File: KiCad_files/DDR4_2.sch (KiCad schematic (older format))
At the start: 16 parts

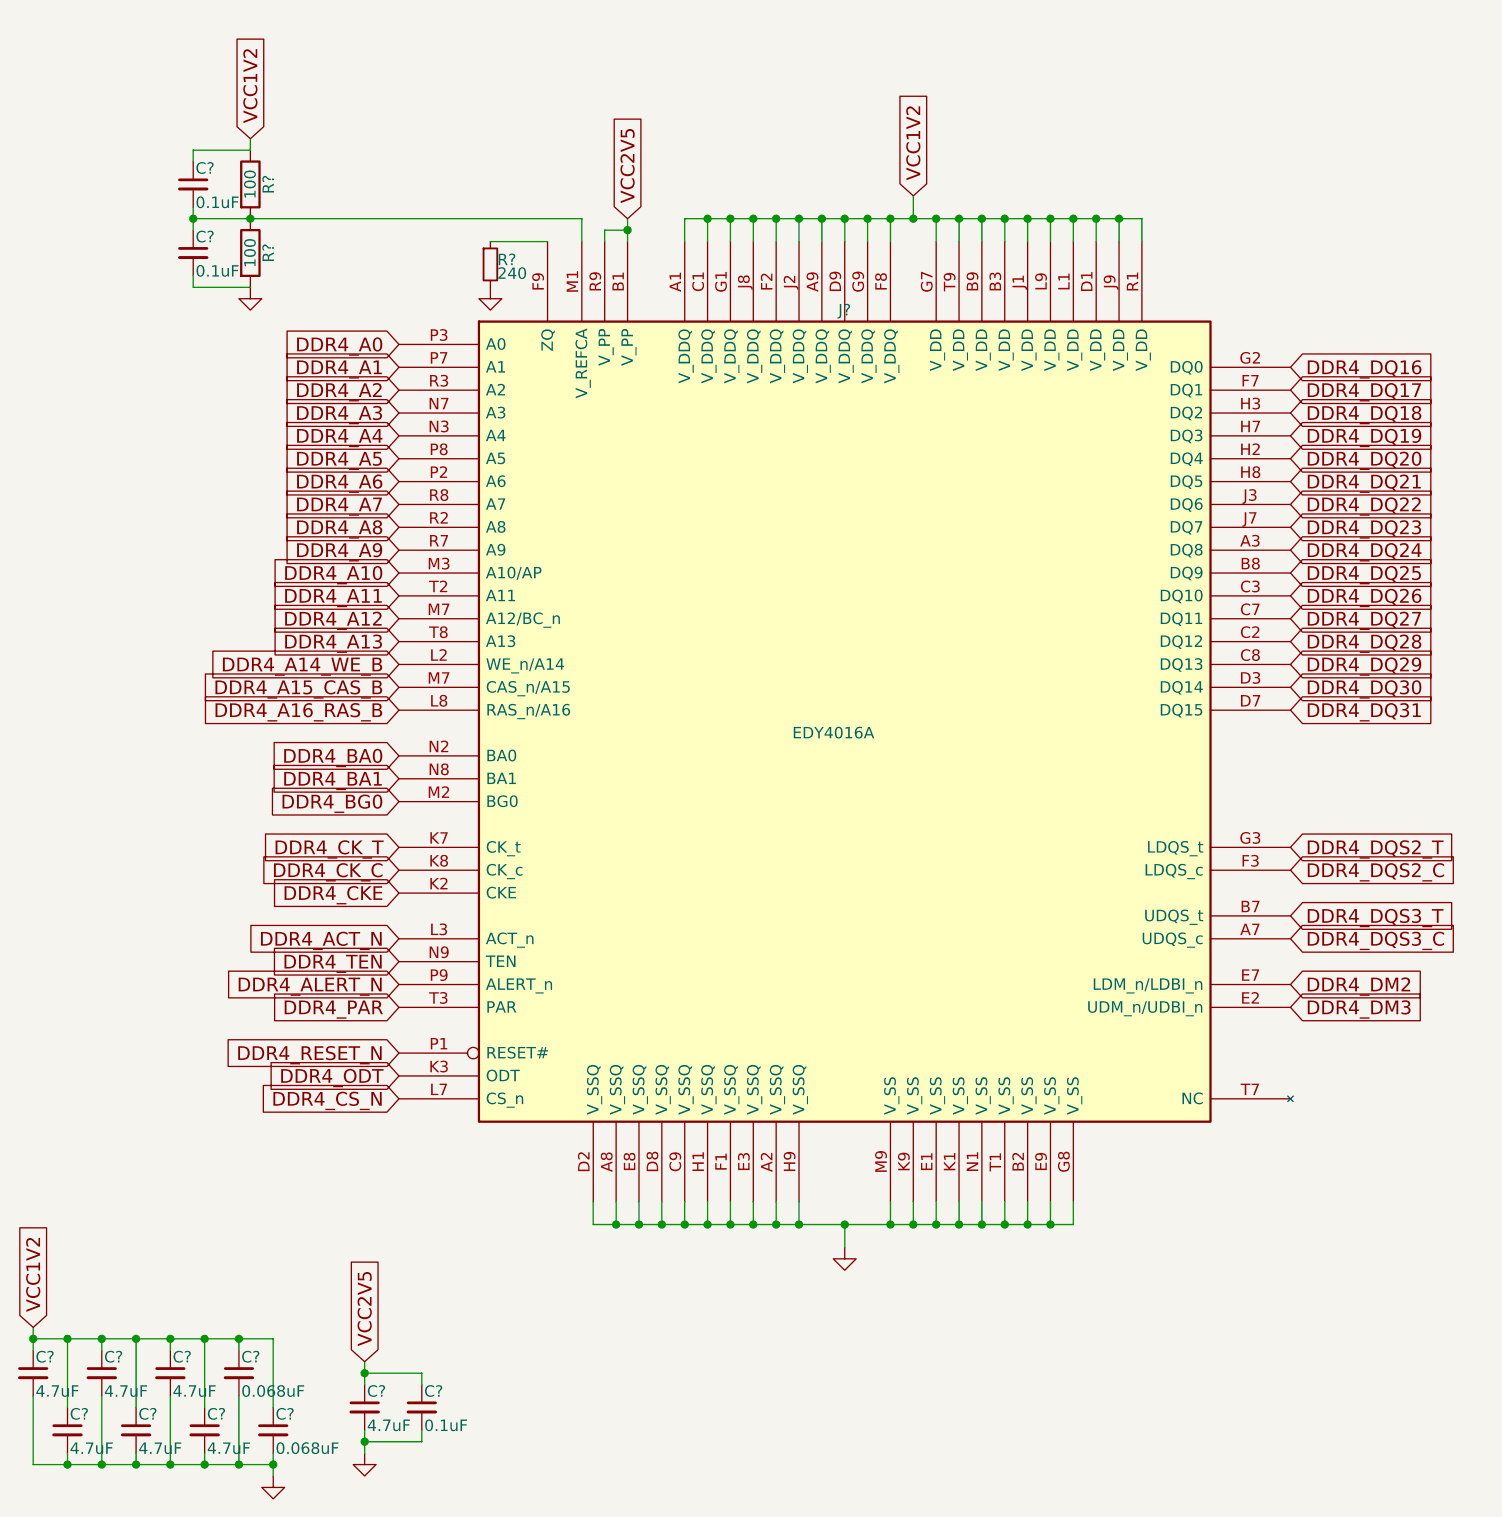
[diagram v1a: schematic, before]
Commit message: Cleanup for demo/presentation
Merged Config and Debug sheets.
Added GPIO for remaining pins.
Annotations.
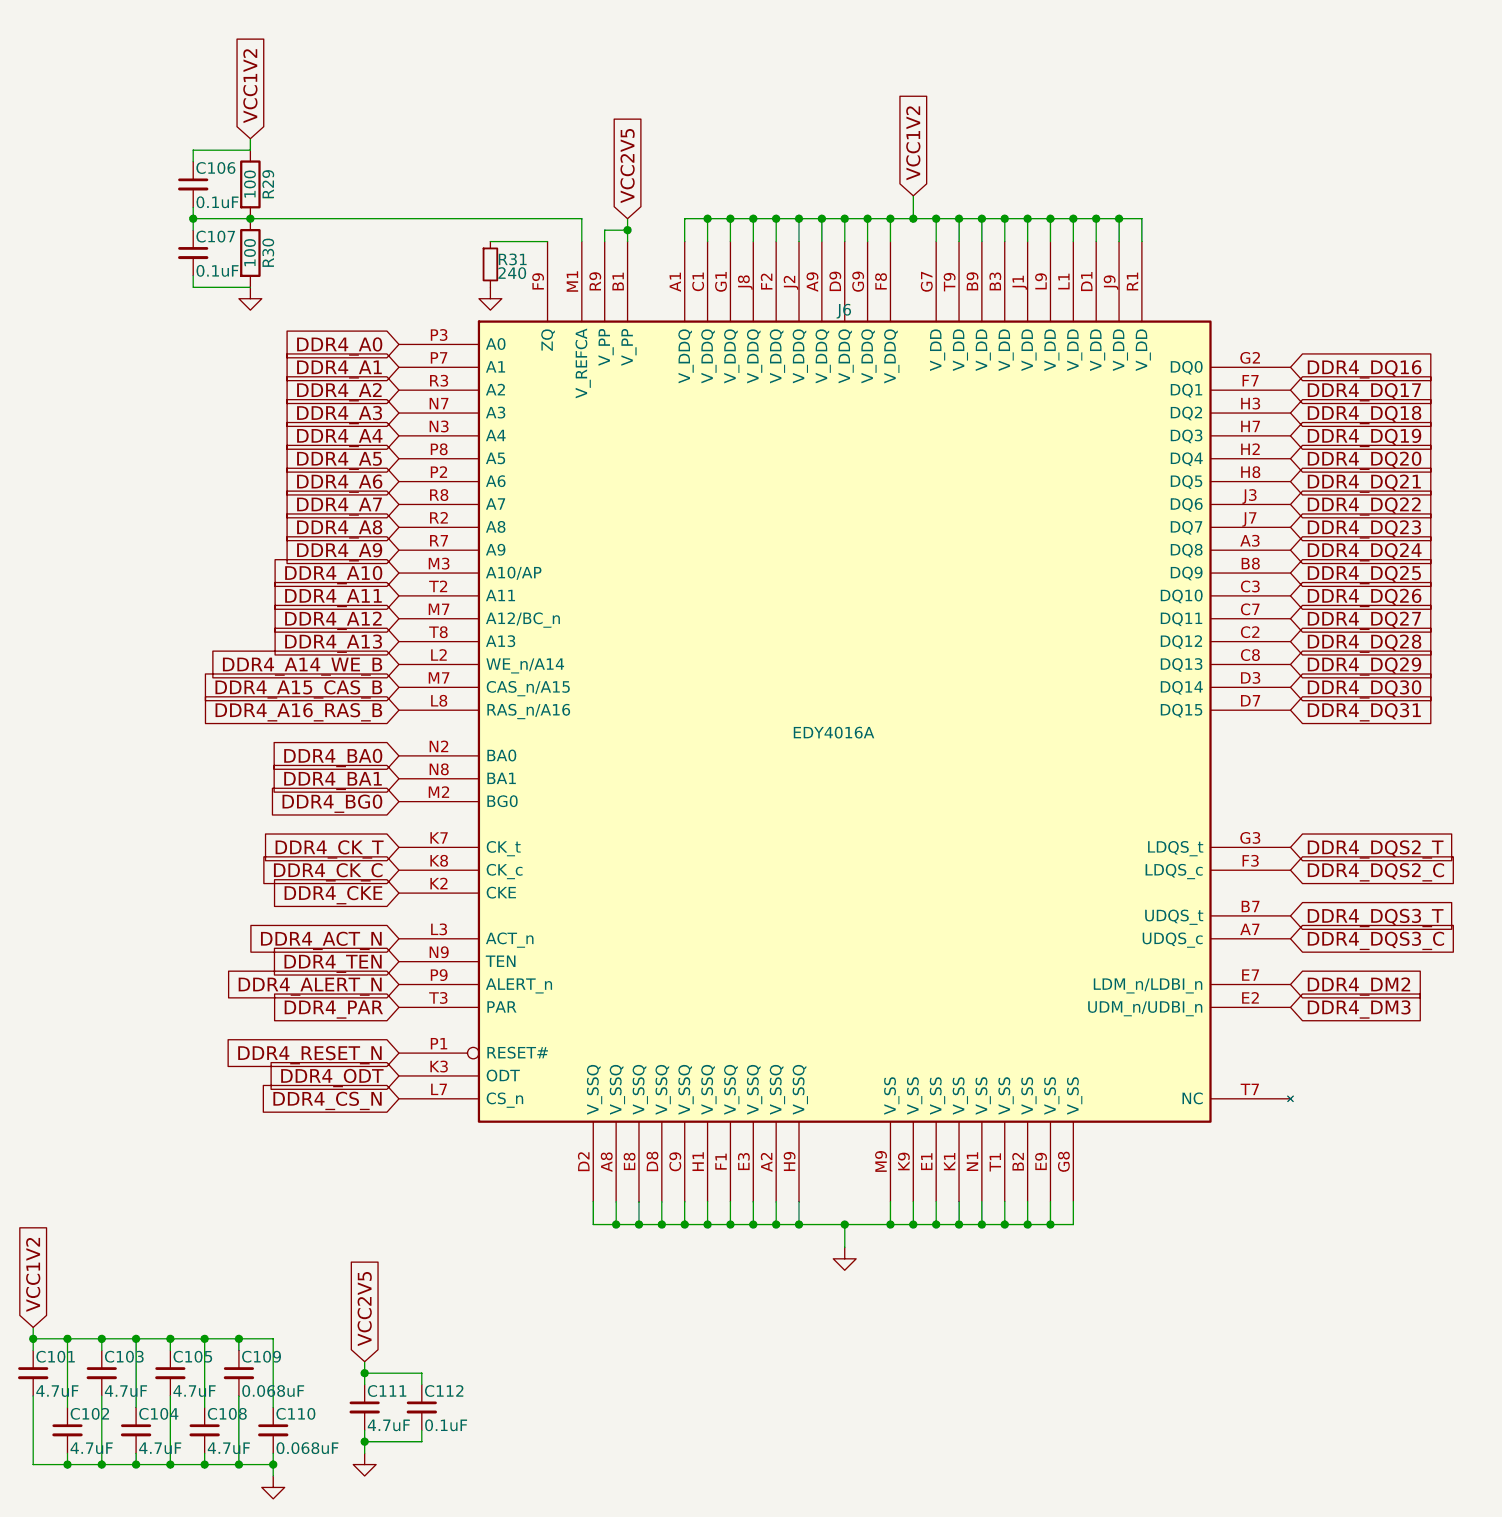
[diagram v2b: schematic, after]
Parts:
- gave numbers to parts that had none: 16
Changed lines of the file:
@@
 $Descr A4 11693 8268
 encoding utf-8
-Sheet 9 10
-Title ""
-Date ""
-Rev ""
-Comp ""
+Sheet 8 10
+Title "Reconfigurable Application-Specific Accelerator Card"
+Date "2018-11-27"
+Rev "1.0"
+Comp "Brian Hong & Jasmine Tang"
 Comment1 ""
-Comment2 ""
-Comment3 ""
-Comment4 ""
+Comment2 "Advisor: Professor Sable"
+Comment3 "Senior Projects"
+Comment4 "The Cooper Union for the Advancement of Science and Art"
 $EndDescr
 $Comp
-L EDY4016A J?
+L EDY4016A J6
 U 1 1 5C14AF0F
 P 6100 4000
-F 0 "J?" H 6100 5850 50  0000 C CNN
+F 0 "J6" H 6100 5850 50  0000 C CNN
 F 1 "EDY4016A" H 6050 4000 50  0000 C CNN
 F 2 "" H 6100 2650 50  0001 C CNN
@@
 VCC2V5
 $Comp
-L R_Small R?
+L R_Small R31
 U 1 1 5C14AF28
 P 4550 1950
-F 0 "R?" H 4580 1970 50  0000 L CNN
+F 0 "R31" H 4580 1970 50  0000 L CNN
 F 1 "240" H 4580 1910 50  0000 L CNN
 F 2 "" H 4550 1950 50  0001 C CNN
@@
 $EndComp
 $Comp
-L GND #PWR?
+L GND #PWR102
 U 1 1 5C14AF2F
 P 4550 2050
-F 0 "#PWR?" H 4550 1800 50  0001 C CNN
+F 0 "#PWR102" H 4550 1800 50  0001 C CNN
 F 1 "GND" H 4550 1900 50  0001 C CNN
 F 2 "" H 4550 2050 50  0001 C CNN
@@
 $EndComp
 $Comp
-L GND #PWR?
+L GND #PWR103
 U 1 1 5C14AF35
 P 6100 6250
-F 0 "#PWR?" H 6100 6000 50  0001 C CNN
+F 0 "#PWR103" H 6100 6000 50  0001 C CNN
 F 1 "GND" H 6100 6100 50  0001 C CNN
 F 2 "" H 6100 6250 50  0001 C CNN
@@
 $EndComp
 $Comp
-L R R?
+L R R29
 U 1 1 5C14AF3B
 P 3500 1600
-F 0 "R?" V 3580 1600 50  0000 C CNN
+F 0 "R29" V 3580 1600 50  0000 C CNN
 F 1 "100" V 3500 1600 50  0000 C CNN
 F 2 "" V 3430 1600 50  0001 C CNN
@@
 $EndComp
 $Comp
-L R R?
+L R R30
 U 1 1 5C14AF42
 P 3500 1900
-F 0 "R?" V 3580 1900 50  0000 C CNN
+F 0 "R30" V 3580 1900 50  0000 C CNN
 F 1 "100" V 3500 1900 50  0000 C CNN
 F 2 "" V 3430 1900 50  0001 C CNN
@@
 $EndComp
 $Comp
-L GND #PWR?
+L GND #PWR99
 U 1 1 5C14AF49
 P 3500 2050
-F 0 "#PWR?" H 3500 1800 50  0001 C CNN
+F 0 "#PWR99" H 3500 1800 50  0001 C CNN
 F 1 "GND" H 3500 1900 50  0001 C CNN
 F 2 "" H 3500 2050 50  0001 C CNN
@@
 VCC1V2
 $Comp
-L C_Small C?
+L C_Small C107
 U 1 1 5C14AF50
 P 3250 1900
-F 0 "C?" H 3260 1970 50  0000 L CNN
+F 0 "C107" H 3260 1970 50  0000 L CNN
 F 1 "0.1uF" H 3260 1820 50  0000 L CNN
 F 2 "" H 3250 1900 50  0001 C CNN
@@
 $EndComp
 $Comp
-L C_Small C?
+L C_Small C106
 U 1 1 5C14AF57
 P 3250 1600
-F 0 "C?" H 3260 1670 50  0000 L CNN
+F 0 "C106" H 3260 1670 50  0000 L CNN
 F 1 "0.1uF" H 3260 1520 50  0000 L CNN
 F 2 "" H 3250 1600 50  0001 C CNN
@@
 VCC1V2
 $Comp
-L GND #PWR?
+L GND #PWR100
 U 1 1 5C14AF84
 P 3600 7250
-F 0 "#PWR?" H 3600 7000 50  0001 C CNN
+F 0 "#PWR100" H 3600 7000 50  0001 C CNN
 F 1 "GND" H 3600 7100 50  0001 C CNN
 F 2 "" H 3600 7250 50  0001 C CNN
@@
 $EndComp
 $Comp
-L C_Small C?
+L C_Small C101
 U 1 1 5C14AF8A
 P 2550 6800
-F 0 "C?" H 2560 6870 50  0000 L CNN
+F 0 "C101" H 2560 6870 50  0000 L CNN
 F 1 "4.7uF" H 2560 6720 50  0000 L CNN
 F 2 "" H 2550 6800 50  0001 C CNN
@@
 $EndComp
 $Comp
-L C_Small C?
+L C_Small C103
 U 1 1 5C14AF91
 P 2850 6800
-F 0 "C?" H 2860 6870 50  0000 L CNN
+F 0 "C103" H 2860 6870 50  0000 L CNN
 F 1 "4.7uF" H 2860 6720 50  0000 L CNN
 F 2 "" H 2850 6800 50  0001 C CNN
@@
 $EndComp
 $Comp
-L C_Small C?
+L C_Small C105
 U 1 1 5C14AF98
 P 3150 6800
-F 0 "C?" H 3160 6870 50  0000 L CNN
+F 0 "C105" H 3160 6870 50  0000 L CNN
 F 1 "4.7uF" H 3160 6720 50  0000 L CNN
 F 2 "" H 3150 6800 50  0001 C CNN
@@
 $EndComp
 $Comp
-L C_Small C?
+L C_Small C109
 U 1 1 5C14AF9F
 P 3450 6800
-F 0 "C?" H 3460 6870 50  0000 L CNN
+F 0 "C109" H 3460 6870 50  0000 L CNN
 F 1 "0.068uF" H 3460 6720 50  0000 L CNN
 F 2 "" H 3450 6800 50  0001 C CNN
@@
 $EndComp
 $Comp
-L C_Small C?
+L C_Small C102
 U 1 1 5C14AFA6
 P 2700 7050
-F 0 "C?" H 2710 7120 50  0000 L CNN
+F 0 "C102" H 2710 7120 50  0000 L CNN
 F 1 "4.7uF" H 2710 6970 50  0000 L CNN
 F 2 "" H 2700 7050 50  0001 C CNN
@@
 $EndComp
 $Comp
-L C_Small C?
+L C_Small C104
 U 1 1 5C14AFAD
 P 3000 7050
-F 0 "C?" H 3010 7120 50  0000 L CNN
+F 0 "C104" H 3010 7120 50  0000 L CNN
 F 1 "4.7uF" H 3010 6970 50  0000 L CNN
 F 2 "" H 3000 7050 50  0001 C CNN
@@
 $EndComp
 $Comp
-L C_Small C?
+L C_Small C108
 U 1 1 5C14AFB4
 P 3300 7050
-F 0 "C?" H 3310 7120 50  0000 L CNN
+F 0 "C108" H 3310 7120 50  0000 L CNN
 F 1 "4.7uF" H 3310 6970 50  0000 L CNN
 F 2 "" H 3300 7050 50  0001 C CNN
@@
 $EndComp
 $Comp
-L C_Small C?
+L C_Small C110
 U 1 1 5C14AFBB
 P 3600 7050
-F 0 "C?" H 3610 7120 50  0000 L CNN
+F 0 "C110" H 3610 7120 50  0000 L CNN
 F 1 "0.068uF" H 3610 6970 50  0000 L CNN
 F 2 "" H 3600 7050 50  0001 C CNN
@@
 Connection ~ 3450 7200
 $Comp
-L C_Small C?
+L C_Small C111
 U 1 1 5C14B041
 P 4000 6950
-F 0 "C?" H 4010 7020 50  0000 L CNN
+F 0 "C111" H 4010 7020 50  0000 L CNN
 F 1 "4.7uF" H 4010 6870 50  0000 L CNN
 F 2 "" H 4000 6950 50  0001 C CNN
@@
 $EndComp
 $Comp
-L GND #PWR?
+L GND #PWR101
 U 1 1 5C14B048
 P 4000 7150
-F 0 "#PWR?" H 4000 6900 50  0001 C CNN
+F 0 "#PWR101" H 4000 6900 50  0001 C CNN
 F 1 "GND" H 4000 7000 50  0001 C CNN
 F 2 "" H 4000 7150 50  0001 C CNN
@@
 $EndComp
 $Comp
-L C_Small C?
+L C_Small C112
 U 1 1 5C14B04E
 P 4250 6950
-F 0 "C?" H 4260 7020 50  0000 L CNN
+F 0 "C112" H 4260 7020 50  0000 L CNN
 F 1 "0.1uF" H 4260 6870 50  0000 L CNN
 F 2 "" H 4250 6950 50  0001 C CNN
